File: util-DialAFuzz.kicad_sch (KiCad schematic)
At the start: 6 parts, among them J1 Conn_01x03_Pin, Q1 BC847, Q2 BC847

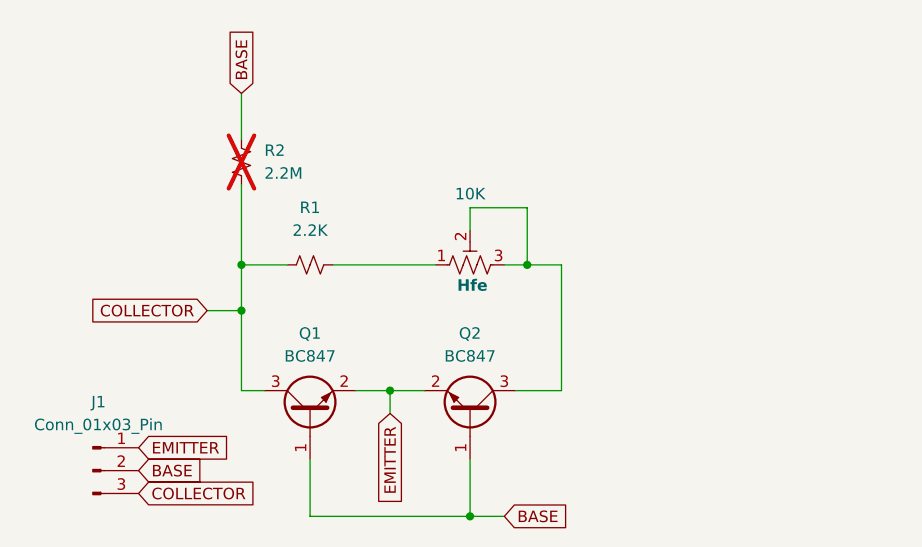
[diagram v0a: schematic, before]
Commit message: Rework as Widlar hFE dial: Q1 diode-connected with 1M emitter trimmer, Q2 pass transistor
The first draft paralleled Q2 with a rheostat in its collector, which does
nothing until Q2 saturates and then collapses the effective hFE. Now Q1 is
diode-connected (C tied to B) with RV1 as a rheostat in its emitter, so it
steals base drive from Q2 in a Widlar split; effective hFE is roughly linear
in RV1 and scales with the host stage's bias current (1M reaches ~125 in a
50 uA collector-feedback stage). R1 dropped: the floor is not a stopper.
R2 2.2M collector-base (DNP) remains the leakage stand-in.

Co-Authored-By: Claude Fable 5.1 <noreply@anthropic.com>
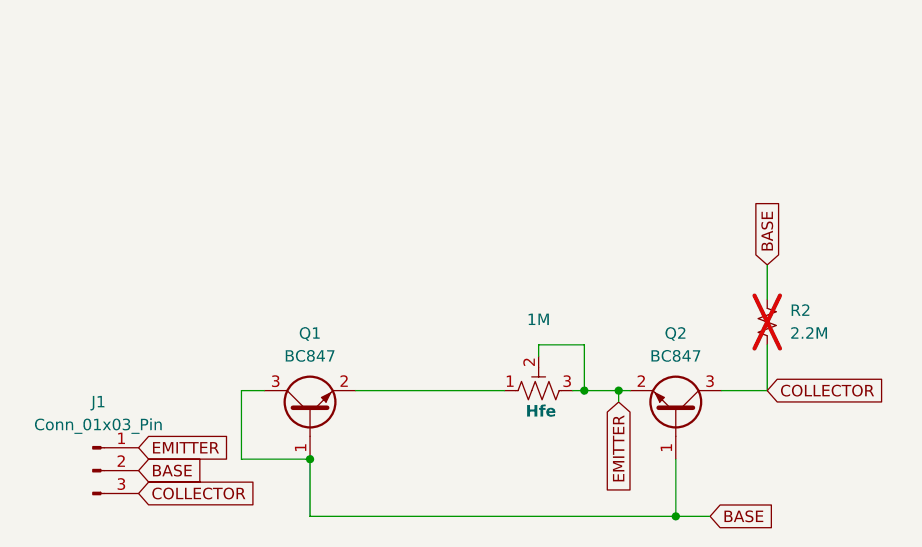
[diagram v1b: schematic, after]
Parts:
- removed R1: 2.2K, Resistor_SMD:R_0805_2012Metric_Pad1.20x1.40mm_HandSolder, symbol Device:R_Small_US
- RV1: value 10K -> 1M
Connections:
- net BASE: now also Q1.3 (C)
- net COLLECTOR: now also Q2.3 (C); no longer Q1.3 (C)
- net EMITTER: now also RV1.2, RV1.3; no longer Q1.2 (E)
- net at RV1.1: now also Q1.2 (E)
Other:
- moved on the sheet: Q2, R2

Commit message: v0.2: compact double-sided layout, trimmer on the back (9.5 x 15.8 mm)
Same Widlar circuit as v0.1; the through-hole trimmer moves to the back
side so the SMD parts and header fit a 5.4 mm shorter board.

Co-Authored-By: Claude Fable 5.1 <noreply@anthropic.com>
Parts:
- R2: now fitted
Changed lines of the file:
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@@
 		(on_board yes)
 		(in_pos_files yes)
-		(dnp yes)
+		(dnp no)
 		(fields_autoplaced yes)
 		(property "Reference" "R2"
